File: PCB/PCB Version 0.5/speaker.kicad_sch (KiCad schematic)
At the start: 4 parts, among them Q1 BSS138

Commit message: schematics nearly done
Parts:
- removed C73: 10u, Capacitor_SMD:C_0805_2012Metric, symbol Device:C
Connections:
- net Spk.-: now also D12.2 (A), Q1.3 (D)
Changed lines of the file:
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@@
 	(wire
 		(pts
-			(xy 107.95 80.01) (xy 116.84 80.01)
+			(xy 107.95 80.01) (xy 144.78 80.01)
 		)
 		(stroke
@@
 		(pts
 			(xy 147.32 66.04) (xy 147.32 77.47)
-		)
-		(stroke
-			(width 0)
-			(type default)
-		)
-	)
-	(wire
-		(pts
-			(xy 124.46 80.01) (xy 144.78 80.01)
 		)
 		(stroke
@@
 		)
 	)
-	(text_box "Q1 acts as a pulldown, D12 is the pullup. Q1's gate is PWMed, so that at the drain of Q1, we get an average of VCC/2. This is then shifted up to VBat due to the coupling capacitor, to remove this DC offset. By adjusting the duty cycle of the PWM, we can either pull Spk.- lower (higher duty cycle) or higher (lower duty cycle), to write our sound samples to Spk.-. Since we are just PWMing the voltage, the inductor smoothes out the current ripple to a triangle wave, and because the PWM is so fast, this triangle wave has an amplitude close enough to 0. This way, we get a DAC without proper DAC hardware. "
+	(text_box "Q1 acts as a pulldown, D12 is the flyback. Q1's gate is PWMed at 44.1kHz. By adjusting the duty cycle of the PWM, we can either pull Spk.- lower (higher duty cycle) or higher (lower duty cycle), to write our sound samples to Spk.-. This way, we get a DAC without proper DAC hardware. Alternatively, we can PWM at lower frequencies to write a raw rectangle wave. "
 		(exclude_from_sim no)
 		(at 22.86 60.96 0)
-		(size 59.69 24.13)
+		(size 59.69 16.51)
 		(stroke
 			(width 0)
@@
 	(label "Spk.+"
 		(at 130.81 63.5 0)
-		(fields_autoplaced yes)
 		(effects
 			(font
@@
 	(label "Spk{+ -}"
 		(at 148.59 66.04 0)
-		(fields_autoplaced yes)
 		(effects
 			(font
@@
 	(label "Spk.-"
 		(at 130.81 80.01 0)
-		(fields_autoplaced yes)
 		(effects
 			(font
@@
 		(shape output)
 		(at 160.02 66.04 0)
-		(fields_autoplaced yes)
 		(effects
 			(font
@@
 		(shape input)
 		(at 93.98 85.09 180)
-		(fields_autoplaced yes)
 		(effects
 			(font
@@
 					(unit 1)
 				)
-			)
-		)
-	)
-	(symbol
-		(lib_id "Device:C")
-		(at 120.65 80.01 90)
-		(unit 1)
-		(exclude_from_sim no)
-		(in_bom yes)
-		(on_board yes)
-		(dnp no)
-		(property "Reference" "C73"
-			(at 118.618 76.2 90)
-			(effects
-				(font
-					(size 1.27 1.27)
-				)
-			)
-		)
-		(property "Value" "10u"
-			(at 123.698 76.2 90)
-			(effects
-				(font
-					(size 1.27 1.27)
-				)
-			)
-		)
-		(property "Footprint" "Capacitor_SMD:C_0805_2012Metric"
-			(at 124.46 79.0448 0)
-			(effects
-				(font
-					(size 1.27 1.27)
-				)
-				(hide yes)
-			)
-		)
-		(property "Datasheet" "~"
-			(at 120.65 80.01 0)
-			(effects
-				(font
-					(size 1.27 1.27)
-				)
-				(hide yes)
-			)
-		)
-		(property "Description" "Unpolarized capacitor"
-			(at 120.65 80.01 0)
-			(effects
-				(font
-					(size 1.27 1.27)
-				)
-				(hide yes)
-			)
-		)
-		(pin "2"
-		)
-		(pin "1"
-		)
-		(instances
-			(project ""
-				(path "/1651f454-30c0-48ea-9fcf-6c96a661786a/b926c428-9140-4272-8a94-263799bff176"
-					(reference "C73")
-					(unit 1)
-				)

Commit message: wip backup
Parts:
- removed JP1: SolderJumper_3_Bridged12, Jumper:SolderJumper-3_P1.3mm_Bridged12_RoundedPad1.0x1.5mm, symbol Jumper:SolderJumper_3_Bridged12
- added JP1: SolderJumper_3_Open, Jumper:SolderJumper-3_P1.3mm_Open_RoundedPad1.0x1.5mm, symbol Jumper:SolderJumper_3_Open
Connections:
- net +10V: now also JP1.3 (B)
- net Spk.+: now also JP1.2 (C)
- net VCC: now also JP1.1 (A)
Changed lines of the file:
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@@
 	)
 	(symbol
-		(lib_id "Jumper:SolderJumper_3_Bridged12")
+		(lib_id "Jumper:SolderJumper_3_Open")
 		(at 107.95 53.34 0)
 		(unit 1)
@@
 		(dnp no)
 		(property "Reference" "JP1"
-			(at 107.95 41.402 0)
+			(at 107.95 42.926 0)
 			(effects
 				(font
@@
 			)
 		)
-		(property "Value" "SolderJumper_3_Bridged12"
-			(at 107.95 43.942 0)
+		(property "Value" "SolderJumper_3_Open"
+			(at 107.95 44.958 0)
 			(effects
 				(font
@@
 			)
 		)
-		(property "Footprint" "Jumper:SolderJumper-3_P1.3mm_Bridged12_RoundedPad1.0x1.5mm"
+		(property "Footprint" "Jumper:SolderJumper-3_P1.3mm_Open_RoundedPad1.0x1.5mm"
 			(at 107.95 53.34 0)
 			(effects
@@
 			)
 		)
-		(property "Description" "3-pole Solder Jumper, pins 1+2 closed/bridged"
+		(property "Description" "Solder Jumper, 3-pole, open"
 			(at 107.95 53.34 0)
 			(effects

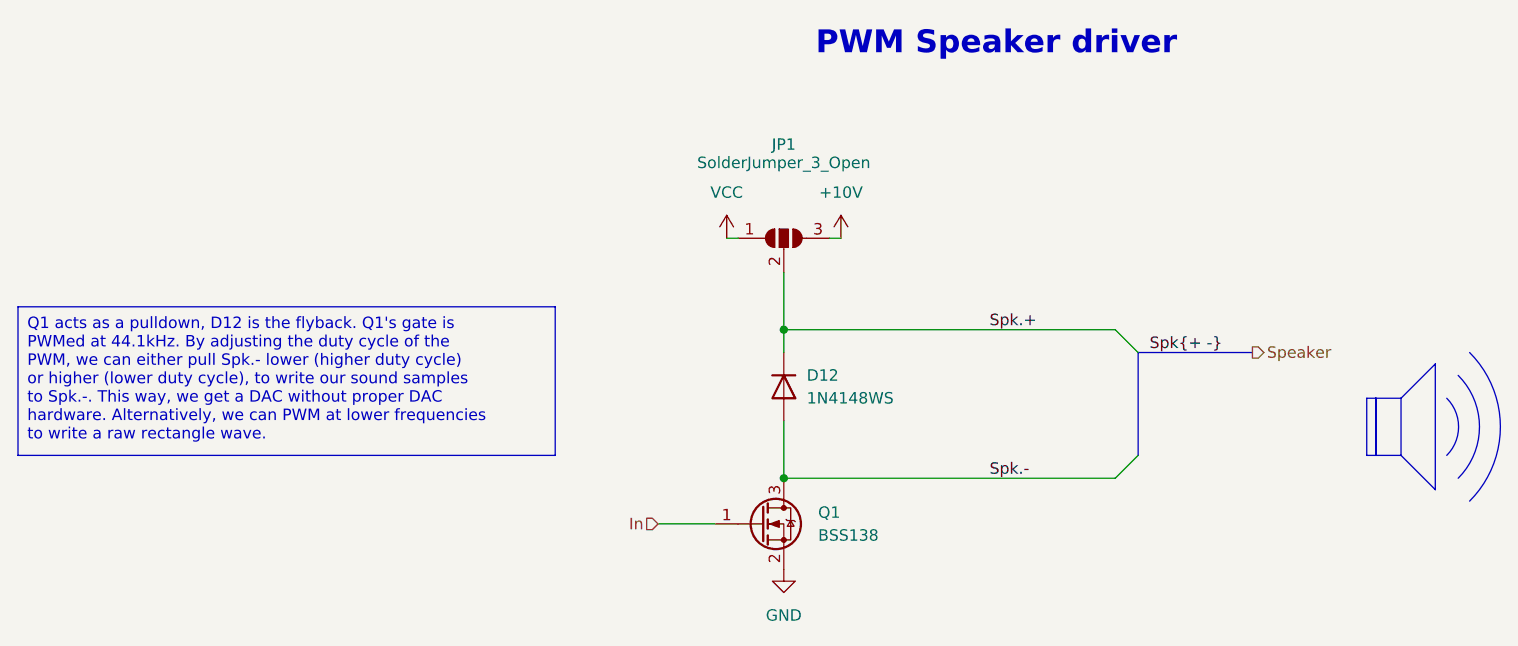
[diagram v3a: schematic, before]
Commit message: preliminary layout
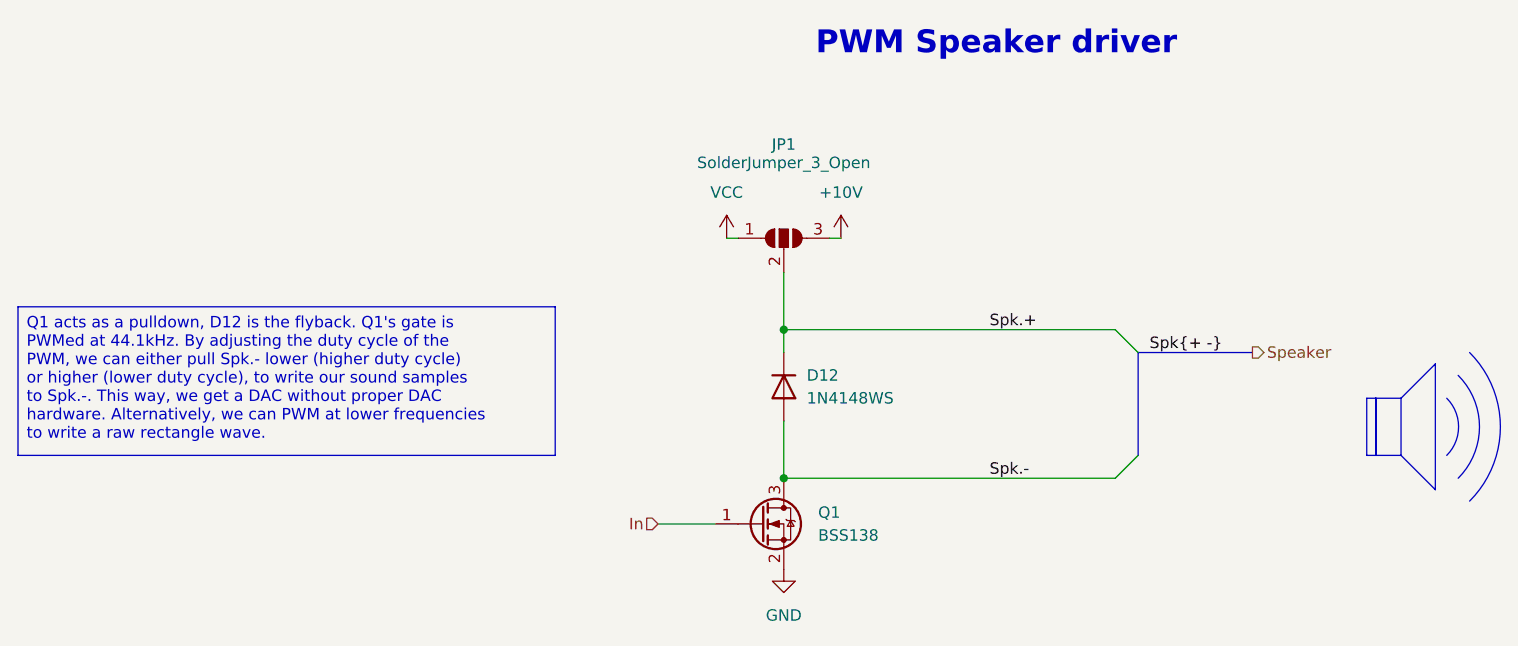
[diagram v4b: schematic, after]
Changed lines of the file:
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@@
 (kicad_sch
-	(version 20231120)
+	(version 20250114)
 	(generator "eeschema")
-	(generator_version "8.0")
+	(generator_version "9.0")
 	(paper "A5")
 	(title_block
 		(title "Kolibri FC - Speaker Driver")
-	)
-	(junction
-		(at 107.95 80.01)
-		(diameter 0)
-		(color 0 0 0 0)
-	)
-	(junction
-		(at 107.95 63.5)
-		(diameter 0)
-		(color 0 0 0 0)
-	)
-	(bus_entry
-		(at 147.32 77.47)
-		(size -2.54 2.54)
-		(stroke
-			(width 0)
-			(type default)
-		)
-	)
-	(bus_entry
-		(at 144.78 63.5)
-		(size 2.54 2.54)
-		(stroke
-			(width 0)
-			(type default)
-		)
-	)
-	(wire
-		(pts
-			(xy 107.95 63.5) (xy 144.78 63.5)
-		)
-		(stroke
-			(width 0)
-			(type default)
-		)
-	)
-	(wire
-		(pts
-			(xy 114.3 53.34) (xy 113.03 53.34)
-		)
-		(stroke
-			(width 0)
-			(type default)
-		)
-	)
-	(bus
-		(pts
-			(xy 147.32 66.04) (xy 160.02 66.04)
-		)
-		(stroke
-			(width 0)
-			(type default)
-		)
-	)
-	(wire
-		(pts
-			(xy 107.95 66.04) (xy 107.95 63.5)
-		)
-		(stroke
-			(width 0)
-			(type default)
-		)
-	)
-	(wire
-		(pts
-			(xy 107.95 73.66) (xy 107.95 80.01)
-		)
-		(stroke
-			(width 0)
-			(type default)
-		)
-	)
-	(wire
-		(pts
-			(xy 107.95 57.15) (xy 107.95 63.5)
-		)
-		(stroke
-			(width 0)
-			(type default)
-		)
-	)
-	(wire
-		(pts
-			(xy 93.98 85.09) (xy 100.33 85.09)
-		)
-		(stroke
-			(width 0)
-			(type default)
-		)
-	)
-	(wire
-		(pts
-			(xy 101.6 53.34) (xy 102.87 53.34)
-		)
-		(stroke
-			(width 0)
-			(type default)
-		)
-	)
-	(wire
-		(pts
-			(xy 107.95 80.01) (xy 144.78 80.01)
-		)
-		(stroke
-			(width 0)
-			(type default)
-		)
-	)
-	(polyline
-		(pts
-			(xy 180.34 67.31) (xy 180.34 81.28)
-		)
-		(stroke
-			(width 0)
-			(type default)
-		)
-	)
-	(polyline
-		(pts
-			(xy 176.53 77.47) (xy 180.34 81.28)
-		)
-		(stroke
-			(width 0)
-			(type default)
-		)
-	)
-	(polyline
-		(pts
-			(xy 176.53 71.12) (xy 180.34 67.31)
-		)
-		(stroke
-			(width 0)
-			(type default)
-		)
-	)
-	(bus
-		(pts
-			(xy 147.32 66.04) (xy 147.32 77.47)
-		)
-		(stroke
-			(width 0)
-			(type default)
-		)
 	)
 	(rectangle
@@
 		(fill
 			(type none)
-		)
-	)
-	(text_box "Q1 acts as a pulldown, D12 is the flyback. Q1's gate is PWMed at 44.1kHz. By adjusting the duty cycle of the PWM, we can either pull Spk.- lower (higher duty cycle) or higher (lower duty cycle), to write our sound samples to Spk.-. This way, we get a DAC without proper DAC hardware. Alternatively, we can PWM at lower frequencies to write a raw rectangle wave. "
-		(exclude_from_sim no)
-		(at 22.86 60.96 0)
-		(size 59.69 16.51)
-		(stroke
-			(width 0)
-			(type default)
-		)
-		(fill
-			(type none)
-		)
-		(effects
-			(font
-				(size 1.27 1.27)
-			)
-			(justify left top)
 		)
 	)
@@
 		)
 	)
+	(text_box "Q1 acts as a pulldown, D12 is the flyback. Q1's gate is PWMed at 44.1kHz. By adjusting the duty cycle of the PWM, we can either pull Spk.- lower (higher duty cycle) or higher (lower duty cycle), to write our sound samples to Spk.-. This way, we get a DAC without proper DAC hardware. Alternatively, we can PWM at lower frequencies to write a raw rectangle wave. "
+		(exclude_from_sim no)
+		(at 22.86 60.96 0)
+		(size 59.69 16.51)
+		(margins 0.9525 0.9525 0.9525 0.9525)
+		(stroke
+			(width 0)
+			(type default)
+		)
+		(fill
+			(type none)
+		)
+		(effects
+			(font
+				(size 1.27 1.27)
+			)
+			(justify left top)
+		)
+	)
+	(junction
+		(at 107.95 80.01)
+		(diameter 0)
+		(color 0 0 0 0)
+	)
+	(junction
+		(at 107.95 63.5)
+		(diameter 0)
+		(color 0 0 0 0)
+	)
+	(bus_entry
+		(at 147.32 77.47)
+		(size -2.54 2.54)
+		(stroke
+			(width 0)
+			(type default)
+		)
+	)
+	(bus_entry
+		(at 144.78 63.5)
+		(size 2.54 2.54)
+		(stroke
+			(width 0)
+			(type default)
+		)
+	)
+	(wire
+		(pts
+			(xy 107.95 63.5) (xy 144.78 63.5)
+		)
+		(stroke
+			(width 0)
+			(type default)
+		)
+	)
+	(wire
+		(pts
+			(xy 114.3 53.34) (xy 113.03 53.34)
+		)
+		(stroke
+			(width 0)
+			(type default)
+		)
+	)
+	(bus
+		(pts
+			(xy 147.32 66.04) (xy 160.02 66.04)
+		)
+		(stroke
+			(width 0)
+			(type default)
+		)
+	)
+	(wire
+		(pts
+			(xy 107.95 66.04) (xy 107.95 63.5)
+		)
+		(stroke
+			(width 0)
+			(type default)
+		)
+	)
+	(wire
+		(pts
+			(xy 107.95 73.66) (xy 107.95 80.01)
+		)
+		(stroke
+			(width 0)
+			(type default)
+		)
+	)
+	(wire
+		(pts
+			(xy 107.95 57.15) (xy 107.95 63.5)
+		)
+		(stroke
+			(width 0)
+			(type default)
+		)
+	)
+	(wire
+		(pts
+			(xy 93.98 85.09) (xy 100.33 85.09)
+		)
+		(stroke
+			(width 0)
+			(type default)
+		)
+	)
+	(wire
+		(pts
+			(xy 101.6 53.34) (xy 102.87 53.34)
+		)
+		(stroke
+			(width 0)
+			(type default)
+		)
+	)
+	(wire
+		(pts
+			(xy 107.95 80.01) (xy 144.78 80.01)
+		)
+		(stroke
+			(width 0)
+			(type default)
+		)
+	)
+	(polyline
+		(pts
+			(xy 180.34 67.31) (xy 180.34 81.28)
+		)
+		(stroke
+			(width 0)
+			(type default)
+		)
+	)
+	(polyline
+		(pts
+			(xy 176.53 77.47) (xy 180.34 81.28)
+		)
+		(stroke
+			(width 0)
+			(type default)
+		)
+	)
+	(polyline
+		(pts
+			(xy 176.53 71.12) (xy 180.34 67.31)
+		)
+		(stroke
+			(width 0)
+			(type default)
+		)
+	)
+	(bus
+		(pts
+			(xy 147.32 66.04) (xy 147.32 77.47)
+		)
+		(stroke
+			(width 0)
+			(type default)
+		)
+	)

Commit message: wip routing
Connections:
- net +10V: now also JP1.1 (A); no longer JP1.3 (B)
- net VCC: now also JP1.3 (B); no longer JP1.1 (A)
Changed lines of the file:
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@@
 	(symbol
 		(lib_id "power:+10V")
-		(at 114.3 53.34 0)
+		(at 101.6 53.34 0)
 		(unit 1)
 		(exclude_from_sim no)
@@
 		(fields_autoplaced yes)
 		(property "Reference" "#PWR0115"
-			(at 114.3 57.15 0)
+			(at 101.6 57.15 0)
 			(effects
 				(font
@@
 		)
 		(property "Value" "+10V"
-			(at 114.3 48.26 0)
+			(at 101.6 48.26 0)
 			(effects
 				(font
@@
 		)
 		(property "Footprint" ""
-			(at 114.3 53.34 0)
+			(at 101.6 53.34 0)
 			(effects
 				(font
@@
 		)
 		(property "Datasheet" ""
-			(at 114.3 53.34 0)
+			(at 101.6 53.34 0)
 			(effects
 				(font
@@
 		)
 		(property "Description" "Power symbol creates a global label with name \"+10V\""
-			(at 114.3 53.34 0)
+			(at 101.6 53.34 0)
 			(effects
 				(font
@@
 		)
 		(instances
-			(project ""
+			(project "Kolibri v0.5"
 				(path "/1651f454-30c0-48ea-9fcf-6c96a661786a/b926c428-9140-4272-8a94-263799bff176"
 					(reference "#PWR0115")
@@
 	(symbol
 		(lib_id "power:VCC")
-		(at 101.6 53.34 0)
+		(at 114.3 53.34 0)
 		(unit 1)
 		(exclude_from_sim no)
@@
 		(fields_autoplaced yes)
 		(property "Reference" "#PWR0114"
-			(at 101.6 57.15 0)
+			(at 114.3 57.15 0)
 			(effects
 				(font
@@
 		)
 		(property "Value" "VCC"
-			(at 101.6 48.26 0)
+			(at 114.3 48.26 0)
 			(effects
 				(font
@@
 		)
 		(property "Footprint" ""
-			(at 101.6 53.34 0)
+			(at 114.3 53.34 0)
 			(effects
 				(font
@@
 		)
 		(property "Datasheet" ""
-			(at 101.6 53.34 0)
+			(at 114.3 53.34 0)
 			(effects
 				(font
@@
 		)
 		(property "Description" "Power symbol creates a global label with name \"VCC\""
-			(at 101.6 53.34 0)
+			(at 114.3 53.34 0)
 			(effects
 				(font
@@
 		)
 		(instances
-			(project ""
+			(project "Kolibri v0.5"
 				(path "/1651f454-30c0-48ea-9fcf-6c96a661786a/b926c428-9140-4272-8a94-263799bff176"
 					(reference "#PWR0114")
